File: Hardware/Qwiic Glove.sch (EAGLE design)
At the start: 24 parts, among them U4 LMV358

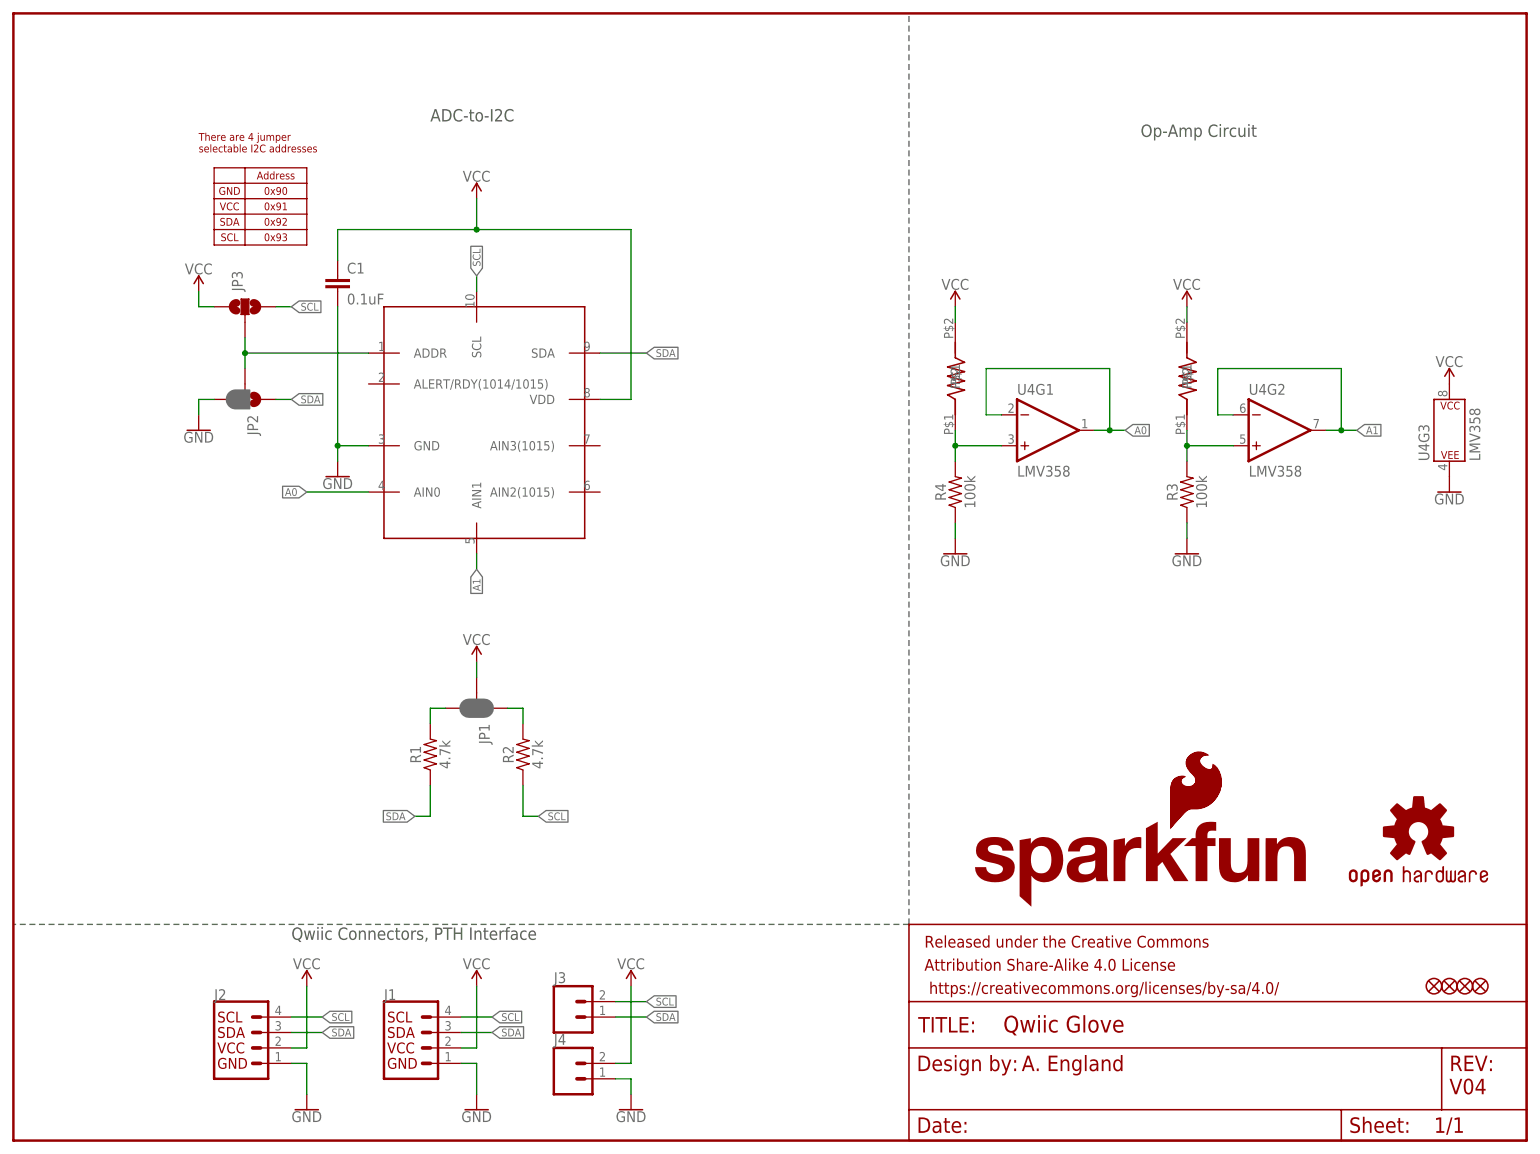
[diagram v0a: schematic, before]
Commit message: updated board to sfe standards
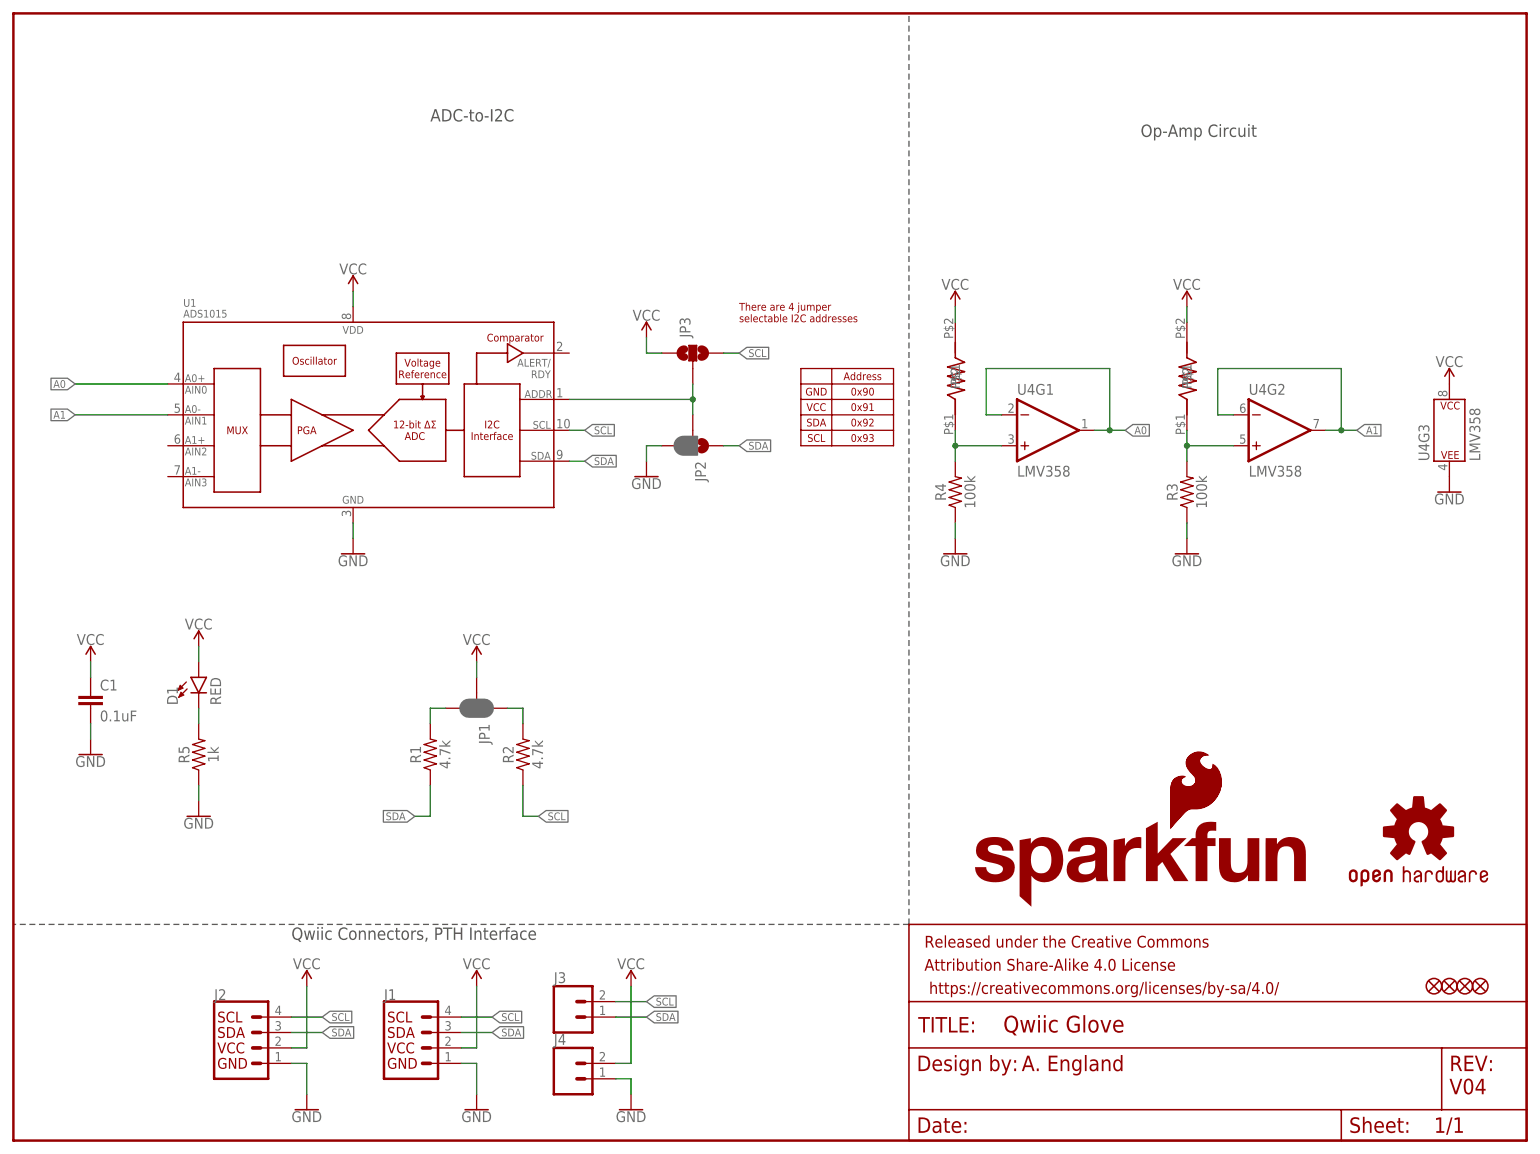
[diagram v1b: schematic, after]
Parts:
- removed U$1: ADS101X-ADC_TO_I2CADS101X, Andy:ADS101X-ADC_TO_I2CADS101X
- added D1: RED, SparkFun-LED:LED-RED0603
- added R5: 1k, SparkFun-Resistors:1KOHM-0603-1/10W-1%
- added U1: ADS1015, SparkFun-IC-Conversion:ADS1015
- J3, J4: device SparkFun-Connectors:CONN_021X02_NO_SILK -> SparkFun-Connectors:CONN_02
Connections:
- new net N$2: D1.C, R5.2
- net A0: now also U1.AIN0; no longer U$1.AIN0
- net A1: now also U1.AIN1; no longer U$1.AIN1
- net GND: now also R5.1, U1.VSS; no longer U$1.GND
- net N$1: now also U1.ADDR; no longer U$1.ADDR
- net SCL: now also U1.SCL; no longer U$1.SCL
- net SDA: now also U1.SDA; no longer U$1.SDA
- net VCC: now also D1.A, U1.VDD; no longer U$1.VDD
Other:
- moved on the sheet: C1, JP2, JP3

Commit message: post checklist changes
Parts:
- removed U$3, U$4: FLEX_SENSOR, Andy:FLEX_SENSOR
- added R6, R7: FLEX_SENSOR-4.5", SparkFun-Resistors:FLEX_SENSOR-4.5"
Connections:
- net N$3: now also R7.1; no longer U$3.P$1
- net N$4: now also R6.1; no longer U$4.P$1
- net VCC: now also R6.2, R7.2; no longer U$3.P$2, U$4.P$2
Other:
- note added: "Clear JP1 to disconnect I2C jumpers."
- note added: "VCC Range: 2.7V-5.5V"
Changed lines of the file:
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@@
 <parts>
 <part name="FRAME1" library="SparkFun-Aesthetics" deviceset="FRAME-LETTER" device=""/>
-<part name="U$3" library="Andy" deviceset="FLEX_SENSOR" device=""/>
 <part name="R3" library="SparkFun-Resistors" deviceset="100KOHM" device="-0603-1/10W-1%" value="100k"/>
 <part name="SUPPLY3" library="SparkFun-PowerSymbols" deviceset="VCC" device=""/>
 <part name="GND3" library="SparkFun-PowerSymbols" deviceset="GND" device=""/>
-<part name="U$4" library="Andy" deviceset="FLEX_SENSOR" device=""/>
 <part name="R4" library="SparkFun-Resistors" deviceset="100KOHM" device="-0603-1/10W-1%" value="100k"/>
 <part name="U4" library="SparkFun-IC-Amplifiers" deviceset="LMV358" device="SOIC" value="LMV358"/>
@@
 <part name="GND10" library="SparkFun-PowerSymbols" deviceset="GND" device=""/>
 <part name="SUPPLY11" library="SparkFun-PowerSymbols" deviceset="VCC" device=""/>
+<part name="R6" library="SparkFun-Resistors" deviceset="FLEX_SENSOR" device="-4.5&quot;"/>
+<part name="R7" library="SparkFun-Resistors" deviceset="FLEX_SENSOR" device="-4.5&quot;"/>
 </parts>
 <sheets>
@@
 <text x="132.08" y="118.11" size="1.27" layer="94" font="vector" align="center">SDA</text>
 <text x="132.08" y="115.57" size="1.27" layer="94" font="vector" align="center">SCL</text>
+<text x="68.58" y="165.1" size="1.778" layer="97" font="vector">VCC Range: 2.7V-5.5V</text>
+<text x="50.8" y="48.26" size="1.778" layer="97" font="vector">Clear JP1 to disconnect I2C jumpers.</text>
 </plain>
 <instances>
 <instance part="FRAME1" gate="G$1" x="0" y="0"/>
 <instance part="FRAME1" gate="V" x="147.32" y="0"/>
-<instance part="U$3" gate="G$1" x="193.04" y="127" rot="R90"/>
 <instance part="R3" gate="G$1" x="193.04" y="106.68" rot="R90"/>
-<instance part="SUPPLY3" gate="G$1" x="193.04" y="137.16"/>
+<instance part="SUPPLY3" gate="G$1" x="193.04" y="129.54"/>
 <instance part="GND3" gate="1" x="193.04" y="96.52"/>
-<instance part="U$4" gate="G$1" x="154.94" y="127" rot="R90"/>
 <instance part="R4" gate="G$1" x="154.94" y="106.68" rot="R90"/>
 <instance part="U4" gate="G1" x="170.18" y="116.84"/>
-<instance part="SUPPLY4" gate="G$1" x="154.94" y="137.16"/>
+<instance part="SUPPLY4" gate="G$1" x="154.94" y="129.54"/>
 <instance part="GND4" gate="1" x="154.94" y="96.52"/>
 <instance part="GND5" gate="1" x="76.2" y="5.08"/>
@@
 <instance part="U4" gate="G2" x="208.28" y="116.84"/>
 <instance part="U4" gate="G3" x="236.22" y="116.84"/>
-<instance part="GND6" gate="1" x="236.22" y="106.68"/>
-<instance part="SUPPLY6" gate="G$1" x="236.22" y="124.46"/>
+<instance part="GND6" gate="1" x="236.22" y="104.14"/>
+<instance part="SUPPLY6" gate="G$1" x="236.22" y="127"/>
 <instance part="J1" gate="G$1" x="66.04" y="15.24"/>
 <instance part="GND1" gate="1" x="12.7" y="63.5"/>
@@
 <instance part="R2" gate="G$1" x="83.82" y="63.5" rot="R90"/>
 <instance part="JP1" gate="G$1" x="76.2" y="71.12" smashed="yes" rot="R270">
-<attribute name="NAME" x="76.581" y="68.58" size="1.778" layer="95" font="vector" rot="R270"/>
+<attribute name="NAME" x="73.66" y="66.421" size="1.778" layer="95" font="vector"/>
 </instance>
 <instance part="SUPPLY2" gate="G$1" x="76.2" y="78.74"/>
@@
 <instance part="J2" gate="G$1" x="38.1" y="15.24"/>
 <instance part="JP2" gate="G$1" x="111.76" y="114.3" smashed="yes" rot="R270">
-<attribute name="NAME" x="112.141" y="111.76" size="1.778" layer="95" font="vector" rot="R270"/>
+<attribute name="NAME" x="109.22" y="109.601" size="1.778" layer="95" font="vector"/>
 </instance>
 <instance part="SUPPLY8" gate="G$1" x="104.14" y="132.08"/>
 <instance part="GND7" gate="1" x="104.14" y="109.22"/>
 <instance part="JP3" gate="G$1" x="111.76" y="129.54" smashed="yes" rot="R90">
-<attribute name="NAME" x="111.379" y="132.08" size="1.778" layer="95" font="vector" rot="R90"/>
+<attribute name="NAME" x="114.3" y="134.239" size="1.778" layer="95" font="vector" rot="R180"/>
 </instance>
 <instance part="LOGO1" gate="G$1" x="157.48" y="38.1"/>
@@
 <instance part="GND10" gate="1" x="30.48" y="53.34"/>
 <instance part="SUPPLY11" gate="G$1" x="30.48" y="81.28"/>
+<instance part="R6" gate="G$1" x="154.94" y="121.92" rot="R90"/>
+<instance part="R7" gate="G$1" x="193.04" y="121.92" rot="R90"/>
 </instances>
 <busses>
@@
 <net name="VCC" class="0">
 <segment>
-<pinref part="U$3" gate="G$1" pin="P$2"/>
 <pinref part="SUPPLY3" gate="G$1" pin="VCC"/>
-<wire x1="193.04" y1="137.16" x2="193.04" y2="134.62" width="0.1524" layer="91"/>
-</segment>
-<segment>
-<pinref part="U$4" gate="G$1" pin="P$2"/>
+<wire x1="193.04" y1="129.54" x2="193.04" y2="127" width="0.1524" layer="91"/>
+<pinref part="R7" gate="G$1" pin="2"/>
+</segment>
+<segment>
 <pinref part="SUPPLY4" gate="G$1" pin="VCC"/>
-<wire x1="154.94" y1="137.16" x2="154.94" y2="134.62" width="0.1524" layer="91"/>
+<wire x1="154.94" y1="129.54" x2="154.94" y2="127" width="0.1524" layer="91"/>
+<pinref part="R6" gate="G$1" pin="2"/>
 </segment>
 <segment>
 <pinref part="U4" gate="G3" pin="P$V+"/>
 <pinref part="SUPPLY6" gate="G$1" pin="VCC"/>
+<wire x1="236.22" y1="127" x2="236.22" y2="124.46" width="0.1524" layer="91"/>
 </segment>
 <segment>
@@
 <pinref part="U4" gate="G3" pin="P$V-"/>
 <pinref part="GND6" gate="1" pin="GND"/>
+<wire x1="236.22" y1="106.68" x2="236.22" y2="109.22" width="0.1524" layer="91"/>
 </segment>
 <segment>
@@
 <net name="N$3" class="0">
 <segment>
-<pinref part="U$3" gate="G$1" pin="P$1"/>
 <wire x1="200.66" y1="114.3" x2="193.04" y2="114.3" width="0.1524" layer="91"/>
 <wire x1="193.04" y1="114.3" x2="193.04" y2="116.84" width="0.1524" layer="91"/>
@@
 <junction x="193.04" y="114.3"/>
 <pinref part="U4" gate="G2" pin="+IN"/>
+<pinref part="R7" gate="G$1" pin="1"/>
 </segment>
 </net>
@@
 <segment>
 <pinref part="U4" gate="G1" pin="+IN"/>
-<pinref part="U$4" gate="G$1" pin="P$1"/>
 <wire x1="162.56" y1="114.3" x2="154.94" y2="114.3" width="0.1524" layer="91"/>
 <wire x1="154.94" y1="114.3" x2="154.94" y2="116.84" width="0.1524" layer="91"/>
@@
 <wire x1="154.94" y1="114.3" x2="154.94" y2="111.76" width="0.1524" layer="91"/>
 <junction x="154.94" y="114.3"/>
-</segment>
-</net>
+<pinref part="R6" gate="G$1" pin="1"/>
+</segment>
+</net>
